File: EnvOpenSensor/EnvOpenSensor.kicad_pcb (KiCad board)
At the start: 2 copper layers, 89.7 x 67.5 mm, 64 parts, among them IC1 IS31FL3730-QFLS2-TR, IC2 IS31FL3730-QFLS2-TR, IC3 IS31FL3730-QFLS2-TR, IC4 IS31FL3730-QFLS2-TR, J1 HRO_TYPE-C-31-M-12, J2 AVR-ISP-6, SW1 SW_Push, SW2 SW_Push, SW3 SW_Push, SW4 SW_Push, U0 TCA9548ARGER, U1 SCD41-D-R2, U2 Si7021-A20, U3 LDO SOT-23-5 3.3V, U4 ATtiny85-20S

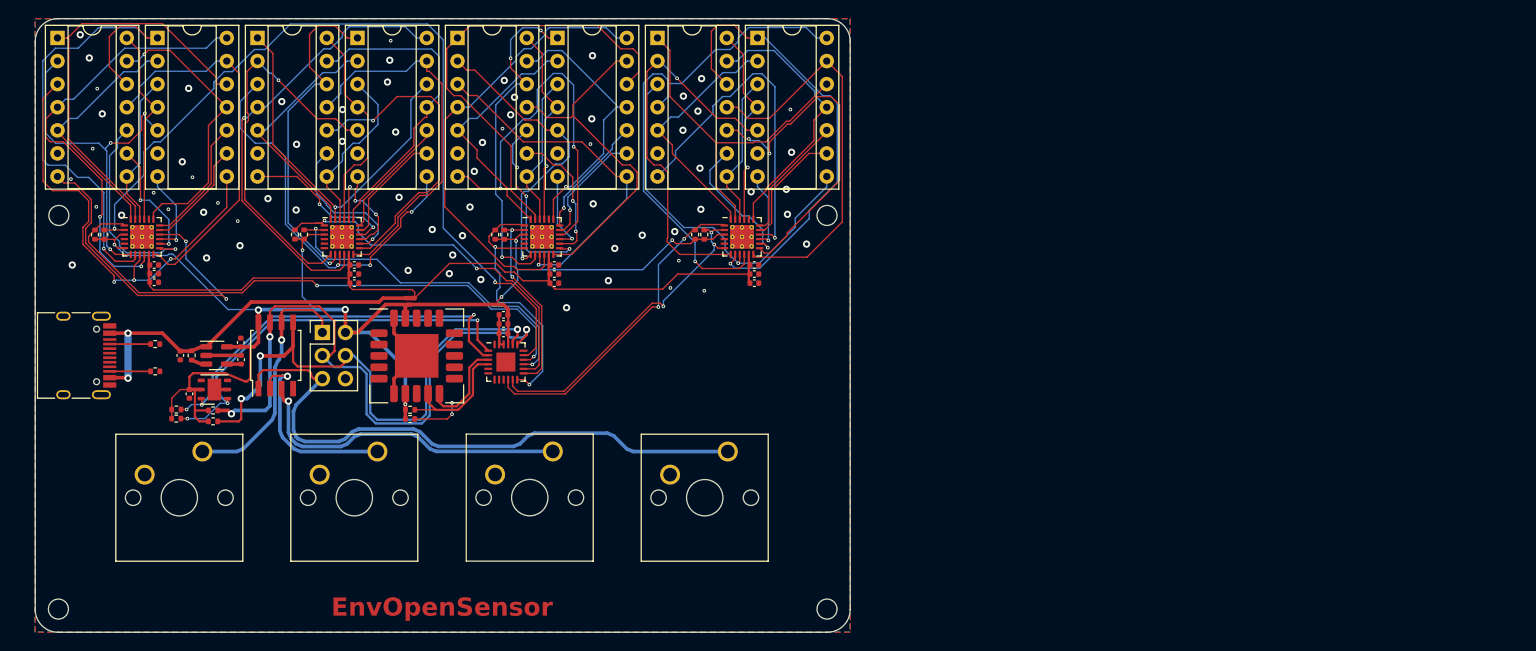
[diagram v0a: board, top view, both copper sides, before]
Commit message: swapped LDO for more capable switching regulator
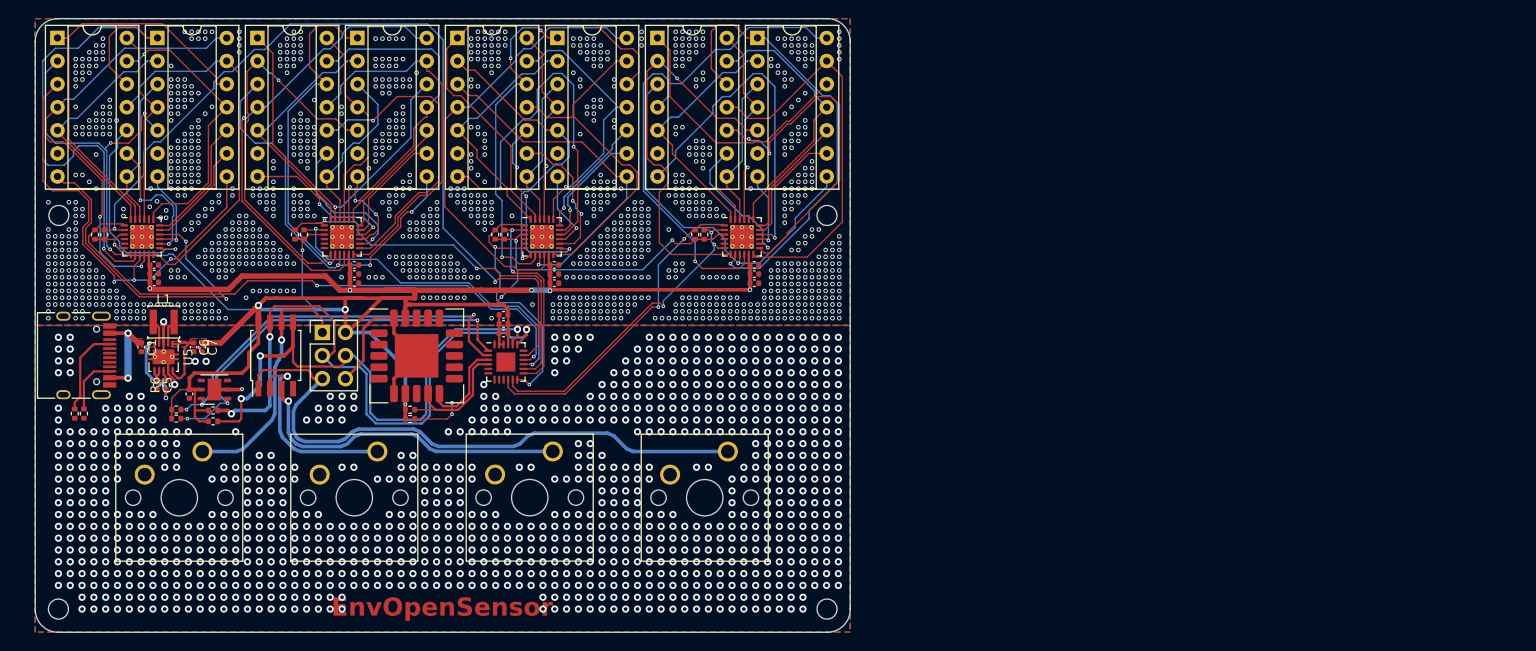
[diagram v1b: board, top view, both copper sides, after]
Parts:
- removed C2, C3, C_BYP_1: 10nF 0402, Capacitor_SMD:C_0402_1005Metric
- removed R3: 10K 0402, Resistor_SMD:R_0402_1005Metric
- removed U3: LDO SOT-23-5 3.3V, Package_TO_SOT_SMD:SOT-23-5
- added C1: 10uF 0402, Capacitor_SMD:C_0402_1005Metric, F.Cu at (26.7, 48.6)
- added C5: 0.1uF 0402, Capacitor_SMD:C_0402_1005Metric, F.Cu at (28.4, 52.8)
- added C6: 10uF 0402, Capacitor_SMD:C_0402_1005Metric, F.Cu at (32.4, 48.6)
- added C7: 10uF 0402, Capacitor_SMD:C_0402_1005Metric, F.Cu at (33.4, 48.6)
- added L1: SPH3015H2R2MT, Inductor_SMD:L_Sunlord_SWPA3015S, F.Cu at (29.1, 45.9)
- added R6: 100ohm 0402, Resistor_SMD:R_0402_1005Metric, F.Cu at (29.4, 52.8)
- added U5: TPS63001DRCR, Package_SON:Texas_DRC0010J_ThermalVias, F.Cu at (29.1, 49.7)
- moved R1 11.7 mm to (19.4, 56.0), turned to -90 degrees
- moved R2 9.12 mm to (20.4, 56.0), turned to -90 degrees
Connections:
- NT0 pad 1: VBUS -> +3V3
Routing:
- net +3V3: track 157.2 -> 198.6 mm
- net VBUS: track 42.7 -> 19.3 mm, vias 2 -> 4
- net GND: track 24.2 -> 41.5 mm, vias 68 -> 2218
- net Net-(J1-CC1): track 4.50 -> 9.75 mm
- net Net-(U5-EN): track 0.00 -> 4.89 mm
- net IC1R2: track 56.9 -> 61.6 mm
- net VCC: track 85.6 -> 89.3 mm, vias 0 -> 5
- net Net-(U5-L2): track 0.00 -> 2.71 mm
- net Net-(U5-L1): track 0.00 -> 2.70 mm
- net SCL7_3V3: track 92.8 -> 95.2 mm
- net IC1R7: track 13.5 -> 15.5 mm
- net SDA6_3V3: track 41.0 -> 43.0 mm
- net Net-(J1-CC2): track 4.50 -> 6.34 mm
- net Net-(U3-EN): track 1.70 -> 0.00 mm
- net SCL5_3V3: track 21.1 -> 22.8 mm
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- added copper zone on F.Cu, net +3V3
- added copper zone on F.Cu, net VBUS

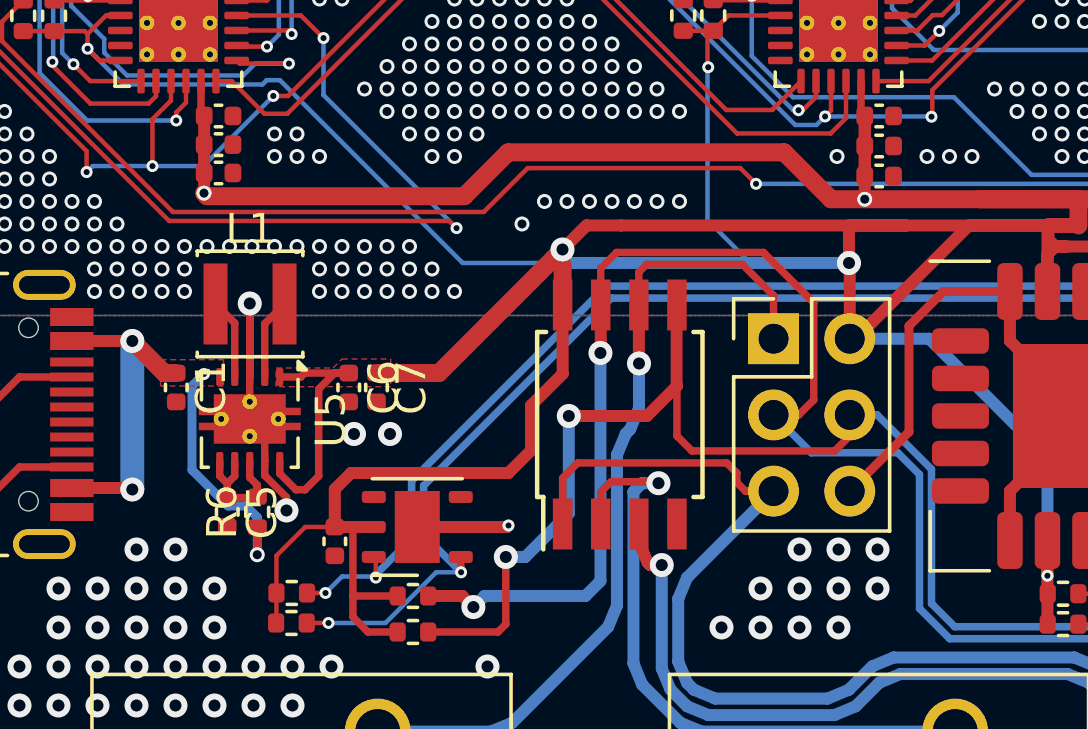
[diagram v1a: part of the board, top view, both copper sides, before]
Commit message: added pin labels and some corrections to layout.
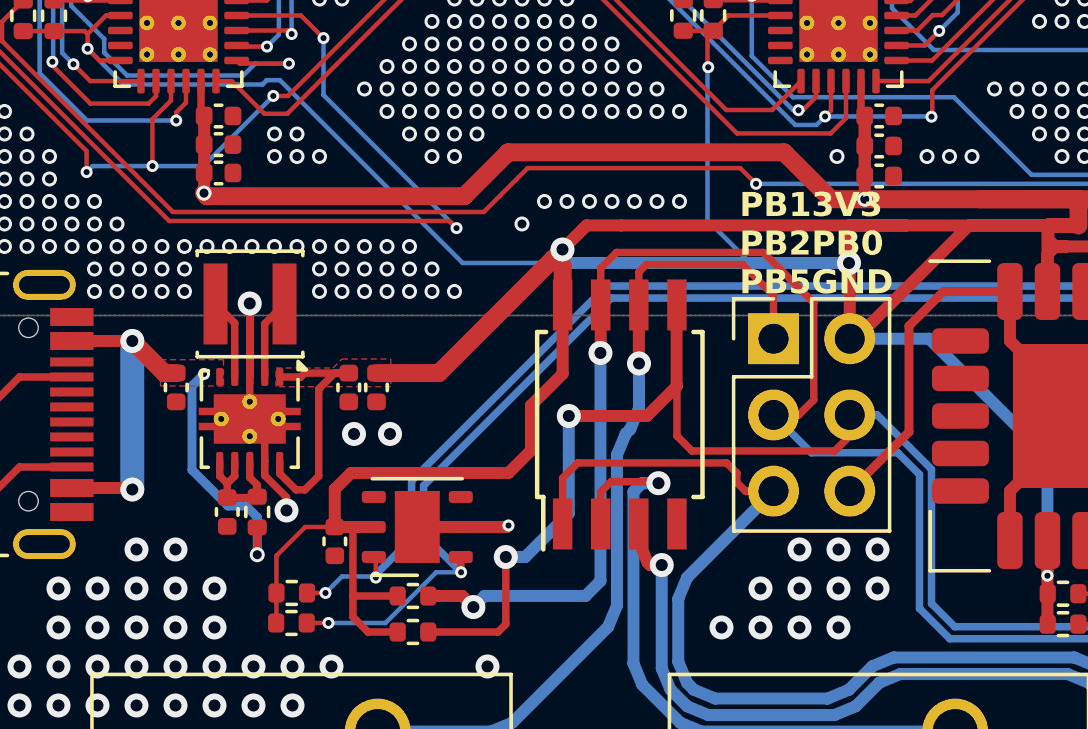
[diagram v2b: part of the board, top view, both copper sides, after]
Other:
- board text added: "3V3 PB0 GND"
- board text added: "PB1 PB2 PB5"

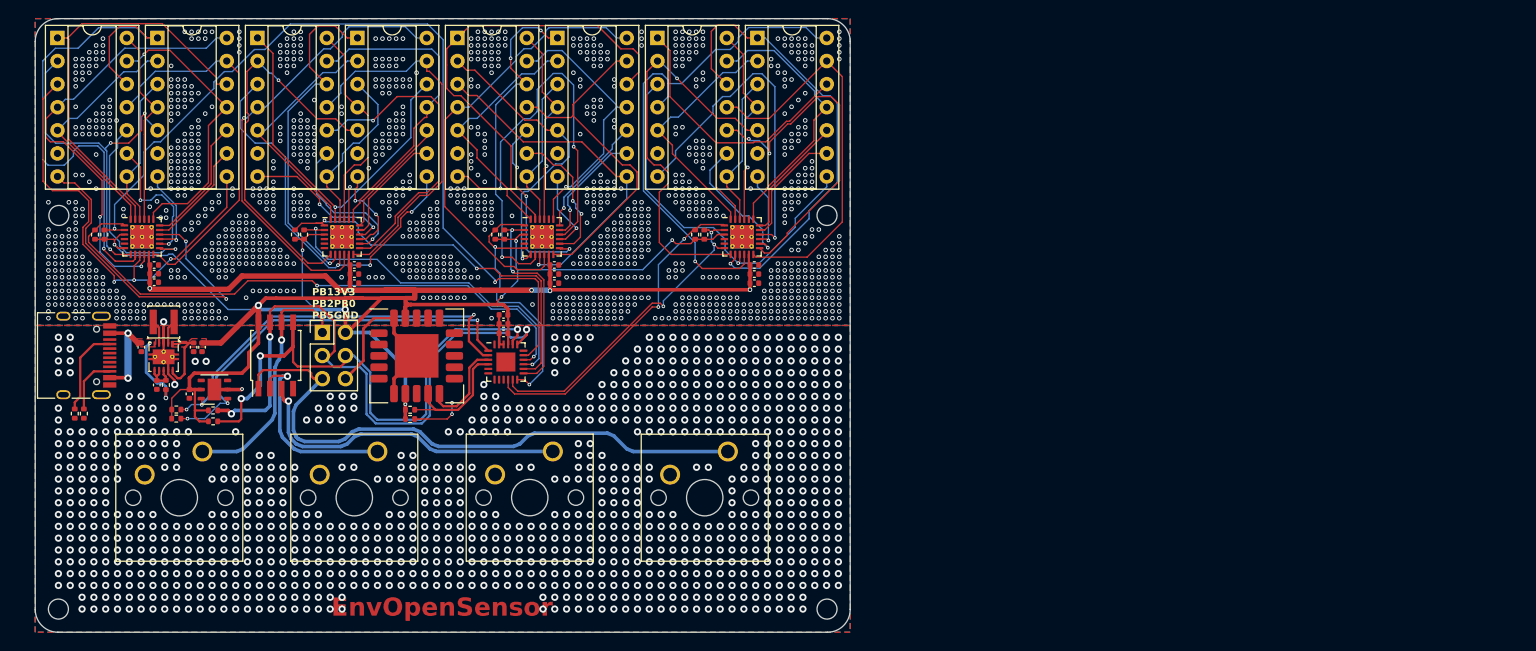
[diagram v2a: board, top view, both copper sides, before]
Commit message: re-drew all traces and moved some components about
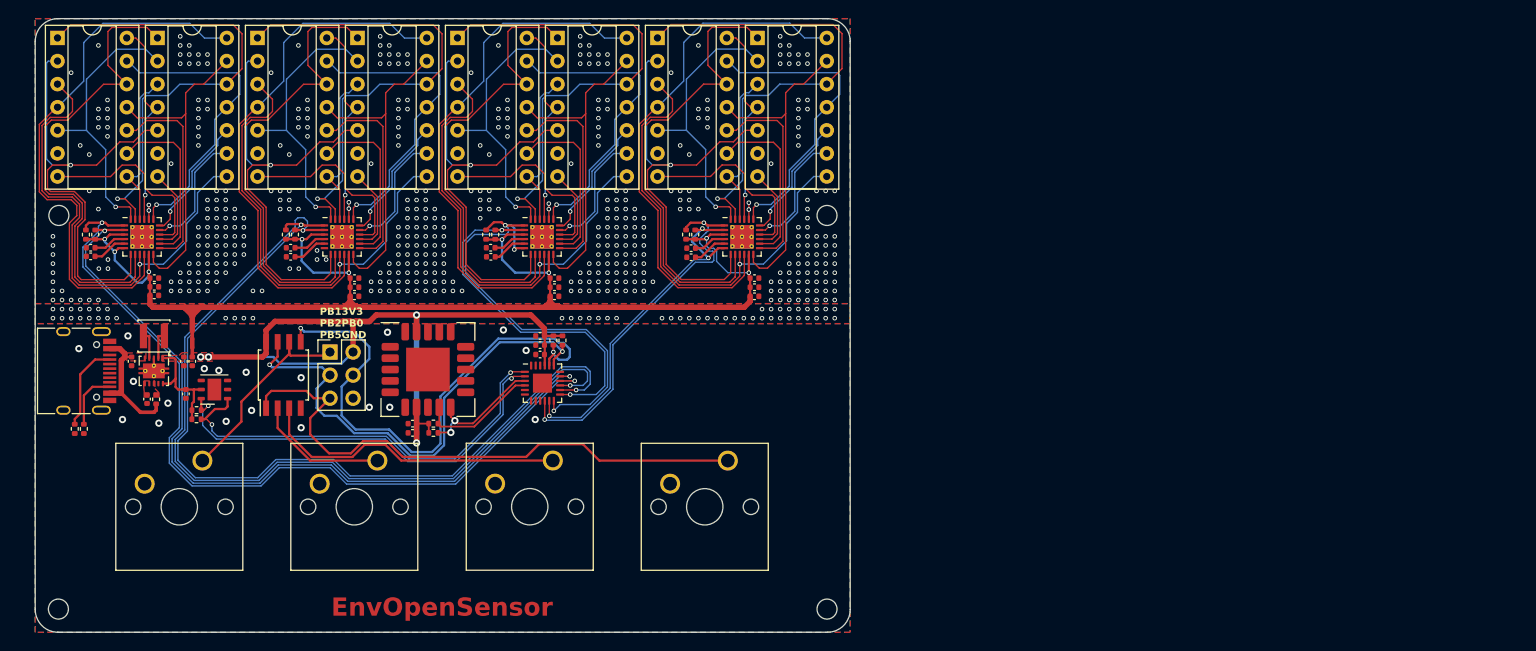
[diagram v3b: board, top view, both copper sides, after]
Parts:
- added C10: 0402 0.22uF, Capacitor_SMD:C_0402_1005Metric, F.Cu at (43.1, 37.7)
- added C11: 0402 0.22uF, Capacitor_SMD:C_0402_1005Metric, F.Cu at (21.1, 37.7)
- added C12: 0402 0.22uF, Capacitor_SMD:C_0402_1005Metric, F.Cu at (65.1, 37.7)
- added C13: 0402 0.22uF, Capacitor_SMD:C_0402_1005Metric, F.Cu at (87.2, 37.8)
- added C14: 0402 1uF, Capacitor_SMD:C_0402_1005Metric, F.Cu at (56.5, 58.1)
- added C15: 0402 10uF, Capacitor_SMD:C_0402_1005Metric, F.Cu at (56.5, 57.0)
- added C2: 0402 0.1uF, Capacitor_SMD:C_0402_1005Metric, F.Cu at (65.1, 38.7)
- added C3: 0402 0.1uF, Capacitor_SMD:C_0402_1005Metric, F.Cu at (21.1, 38.6)
- added C8: 0402 0.1uF, Capacitor_SMD:C_0402_1005Metric, F.Cu at (43.1, 38.7)
- added C9: 0402 0.1uF, Capacitor_SMD:C_0402_1005Metric, F.Cu at (87.2, 38.8)
- moved R5 39.2 mm to (73.0, 47.9), turned to -90 degrees
- moved R4 38.5 mm to (72.0, 47.9), turned to -90 degrees
- moved NT0 24.5 mm to (32.3, 48.2), turned to 90 degrees
- moved C16 4.65 mm to (70.5, 49.5)
- moved U0 4.65 mm to (70.8, 52.6)
- moved C17 4.65 mm to (70.5, 48.4)
- moved C18 4.65 mm to (70.5, 47.4)
- moved R13 2.98 mm to (58.8, 58.1)
- moved R14 2.98 mm to (58.8, 57.0)
- moved U4 2.31 mm to (42.3, 51.7)
- moved J2 2.31 mm to (47.4, 49.2)
- moved R15 2.23 mm to (32.7, 56.6)
- moved R16 2.23 mm to (32.8, 55.6)
- moved U1 1.94 mm to (58.2, 51.1)
- moved R6 1.90 mm to (28.3, 54.4)
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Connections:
- IC1 pad 3: +3V3 -> VCC
- IC1 pad 4: unconnected-(IC1-IN-Pad4) -> Net-(IC1-IN)
- IC1 pad 5: unconnected-(IC1-C_FILT-Pad5) -> Net-(IC1-C_FILT)
- IC1 pad 6: +3V3 -> VCC
- IC2 pad 3: +3V3 -> VCC
- IC2 pad 4: unconnected-(IC2-IN-Pad4) -> Net-(IC2-IN)
- IC2 pad 5: unconnected-(IC2-C_FILT-Pad5) -> Net-(IC2-C_FILT)
- IC3 pad 3: +3V3 -> VCC
- IC3 pad 4: unconnected-(IC3-IN-Pad4) -> Net-(IC3-IN)
- IC3 pad 5: unconnected-(IC3-C_FILT-Pad5) -> Net-(IC3-C_FILT)
- IC4 pad 3: +3V3 -> VCC
- IC4 pad 4: unconnected-(IC4-IN-Pad4) -> Net-(IC4-IN)
- IC4 pad 5: unconnected-(IC4-C_FILT-Pad5) -> Net-(IC4-C_FILT)
- R101 pad 2: +3V3 -> VCC
- R102 pad 2: +3V3 -> VCC
- R103 pad 2: +3V3 -> VCC
- R104 pad 2: +3V3 -> VCC
- R105 pad 2: +3V3 -> VCC
- R106 pad 2: +3V3 -> VCC
- R107 pad 2: +3V3 -> VCC
- R108 pad 2: +3V3 -> VCC
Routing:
- net +3V3: track 198.6 -> 106.3 mm, vias 8 -> 4
- net VCC: track 89.3 -> 149.4 mm, vias 5 -> 9
- net SCL6_3V3: track 38.0 -> 95.3 mm
- net SDA6_3V3: track 43.0 -> 94.3 mm
- net GND: track 41.5 -> 8.92 mm, vias 2218 -> 526
- net SDA7_3V3: track 64.1 -> 90.7 mm
- net IC3C8: track 41.3 -> 21.4 mm, vias 2 -> 0
- net SDA5_3V3: track 30.3 -> 50.0 mm, vias 2 -> 3
- net IC1C8: track 39.2 -> 21.4 mm, vias 2 -> 0
- net IC3R1: track 32.7 -> 50.1 mm
- net SCL5_3V3: track 22.8 -> 39.8 mm
- net IC4C8: track 37.6 -> 21.4 mm, vias 1 -> 0
- net IC4R6: track 38.2 -> 22.4 mm, vias 2 -> 0
- net IC4C2: track 38.3 -> 53.6 mm, vias 0 -> 1
- net PB2: track 68.3 -> 54.8 mm, vias 3 -> 2
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- added copper zone on F.Cu, net Net-(U5-EN)
